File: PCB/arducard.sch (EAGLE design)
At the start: 93 parts, among them J1 USB MICRO, J3 051296-4094, J4 M02PTH, Q1 BSS84, Q10 DMG2301U-7, Q2 BC817-16LT1SMD, Q3 DMG2301U-7, Q4 2N7002, Q5 BSS84, Q6 2N7002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

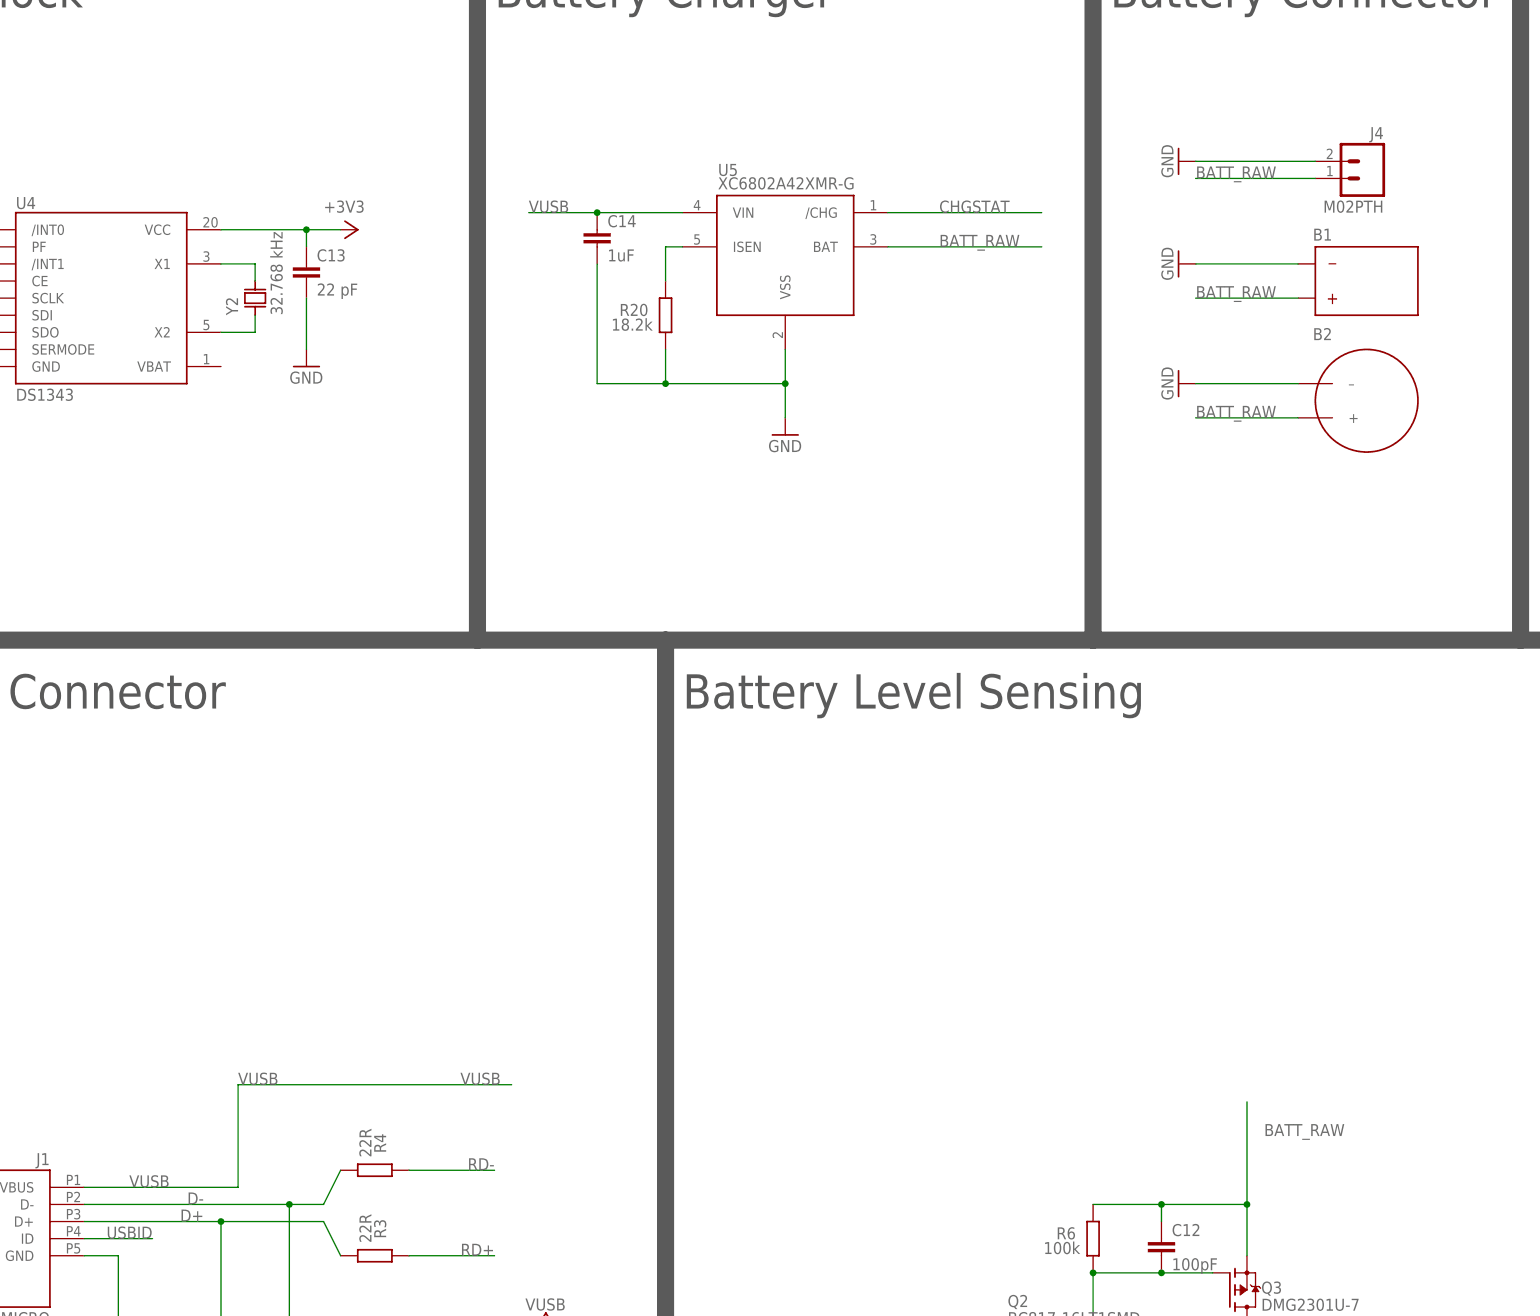
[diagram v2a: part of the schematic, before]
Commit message: removed flat cell battery connector
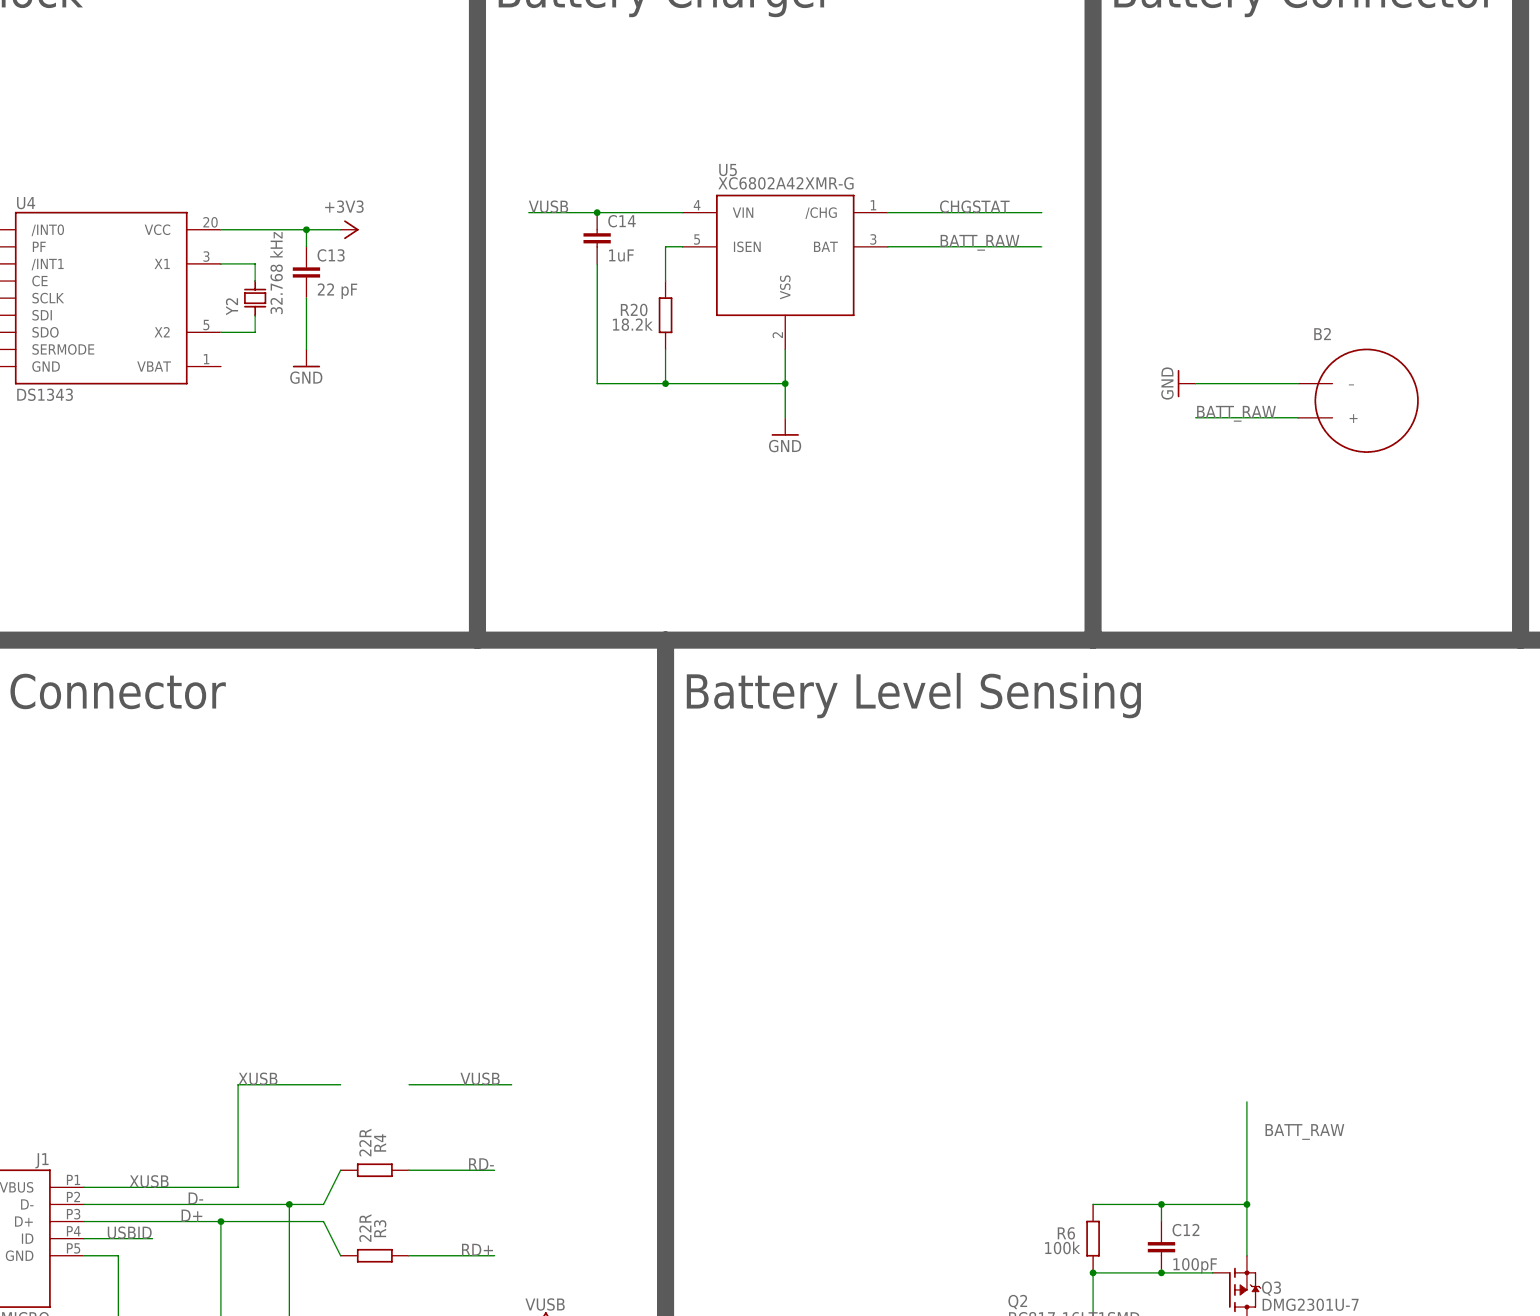
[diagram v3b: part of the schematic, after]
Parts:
- removed B1: PGEB016144, arducard-battery:PGEB016144
- removed J4: M02PTH, SparkFun-Connectors:M02PTH
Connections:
- new net XUSB: J1.VBUS
- net BATT_RAW: no longer B1.+, J4.1
- net GND: no longer B1.-, J4.2
- net VUSB: no longer J1.VBUS
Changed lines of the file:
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@@
 <part name="GND28" library="supply1" deviceset="GND" device=""/>
 <part name="R20" library="SmartPrj" deviceset="R-EU_" device="R0603" value="18.2k"/>
-<part name="GND9" library="supply1" deviceset="GND" device=""/>
-<part name="J4" library="SparkFun-Connectors" deviceset="M02" device="PTH"/>
-<part name="GND10" library="supply1" deviceset="GND" device=""/>
 <part name="GND4" library="supply1" deviceset="GND" device=""/>
 <part name="GND29" library="supply1" deviceset="GND" device=""/>
@@
 <part name="U5" library="arducard-xc6802" deviceset="XC6802A42XMR-G" device=""/>
 <part name="U2" library="v-reg-micrel" deviceset="MIC5219XX" device=""/>
-<part name="B1" library="arducard-battery" deviceset="PGEB016144" device=""/>
 <part name="B2" library="arducard-coincell" deviceset="LIR2016" device=""/>
 <part name="U$1" library="MyPOW" deviceset="VUSB" device=""/>
@@
 <attribute name="VALUE" x="343.535" y="240.792" size="1.778" layer="96" rot="R180"/>
 </instance>
-<instance part="GND9" gate="1" x="421.64" y="248.92" rot="R270"/>
-<instance part="J4" gate="G$1" x="449.58" y="261.62" rot="MR0"/>
-<instance part="GND10" gate="1" x="421.64" y="264.16" rot="R270"/>
 <instance part="GND4" gate="1" x="83.82" y="81.28" rot="R270"/>
 <instance part="GND29" gate="1" x="81.28" y="116.84"/>
@@
 <instance part="U5" gate="XC6802A42XMR-G" x="363.22" y="254"/>
 <instance part="U2" gate="G1" x="543.56" y="243.84"/>
-<instance part="B1" gate="G$1" x="449.58" y="246.38"/>
 <instance part="B2" gate="G$1" x="449.58" y="228.6"/>
 <instance part="U$1" gate="G$1" x="495.3" y="251.46"/>
@@
 <junction x="345.44" y="231.14"/>
 <pinref part="U5" gate="XC6802A42XMR-G" pin="VSS"/>
-</segment>
-<segment>
-<pinref part="GND9" gate="1" pin="GND"/>
-<wire x1="424.18" y1="248.92" x2="439.42" y2="248.92" width="0.1524" layer="91"/>
-<pinref part="B1" gate="G$1" pin="-"/>
-</segment>
-<segment>
-<pinref part="J4" gate="G$1" pin="2"/>
-<pinref part="GND10" gate="1" pin="GND"/>
-<wire x1="441.96" y1="264.16" x2="424.18" y2="264.16" width="0.1524" layer="91"/>
 </segment>
 <segment>
@@
 </segment>
 </net>
-<net name="VUSB" class="3">
+<net name="VUSB" class="0">
 <segment>
 <wire x1="114.3" y1="60.96" x2="104.14" y2="60.96" width="0.1524" layer="91"/>
@@
 </segment>
 <segment>
+<wire x1="322.58" y1="127" x2="307.34" y2="127" width="0.1524" layer="91"/>
+<label x="314.96" y="127" size="1.778" layer="95"/>
+</segment>
+<segment>
 <wire x1="347.98" y1="256.54" x2="335.28" y2="256.54" width="0.1524" layer="91"/>
 <pinref part="C14" gate="G$1" pin="1"/>
@@
 <pinref part="U$12" gate="G$1" pin="VUSB"/>
 <wire x1="518.16" y1="259.08" x2="518.16" y2="261.62" width="0.1524" layer="91"/>
-</segment>
-<segment>
-<wire x1="281.94" y1="111.76" x2="281.94" y2="127" width="0.1524" layer="91"/>
-<wire x1="281.94" y1="127" x2="322.58" y2="127" width="0.1524" layer="91"/>
-<wire x1="259.08" y1="111.76" x2="281.94" y2="111.76" width="0.1524" layer="91"/>
-<label x="271.78" y="111.76" size="1.778" layer="95" rot="MR0"/>
-<label x="281.94" y="127" size="1.778" layer="95"/>
-<pinref part="J1" gate="G$1" pin="VBUS"/>
-<label x="314.96" y="127" size="1.778" layer="95"/>
 </segment>
 </net>
@@
 <pinref part="J1" gate="G$1" pin="D+"/>
 <pinref part="R3" gate="G$1" pin="1"/>
+</segment>
+</net>
+<net name="XUSB" class="3">
+<segment>
+<wire x1="281.94" y1="111.76" x2="281.94" y2="127" width="0.1524" layer="91"/>
+<wire x1="281.94" y1="127" x2="297.18" y2="127" width="0.1524" layer="91"/>
+<wire x1="259.08" y1="111.76" x2="281.94" y2="111.76" width="0.1524" layer="91"/>
+<label x="271.78" y="111.76" size="1.778" layer="95" rot="MR0"/>
+<label x="281.94" y="127" size="1.778" layer="95"/>
+<pinref part="J1" gate="G$1" pin="VBUS"/>
 </segment>
 </net>
@@
 </segment>
 <segment>
-<wire x1="439.42" y1="243.84" x2="424.18" y2="243.84" width="0.1524" layer="91"/>
-<label x="424.18" y="243.84" size="1.778" layer="95"/>
-<pinref part="B1" gate="G$1" pin="+"/>
-</segment>
-<segment>
-<pinref part="J4" gate="G$1" pin="1"/>
-<wire x1="441.96" y1="261.62" x2="424.18" y2="261.62" width="0.1524" layer="91"/>
-<label x="424.18" y="261.62" size="1.778" layer="95"/>
-</segment>
-<segment>

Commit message: initial routing for dorkbot
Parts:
- removed L1: MH2029-300Y, wuerth-elektronik:WE-CBF_0805
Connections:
- removed net N$10: C10.1, D1.C, Q1.S, U2.EN, U2.IN
- removed net XUSB: J1.VBUS
- new net 5V: C10.1, C14.1, D1.C, Q1.S, U1.VBUS, U2.EN, U2.IN, U5.VIN
- net GND: no longer L1.1, L1.2
- net VUSB: now also J1.VBUS; no longer C14.1, U1.VBUS, U5.VIN
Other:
- note removed: "MicroSD Connector"
- moved on the sheet: D1, SW0, SW1, SW2, SW3, SW4

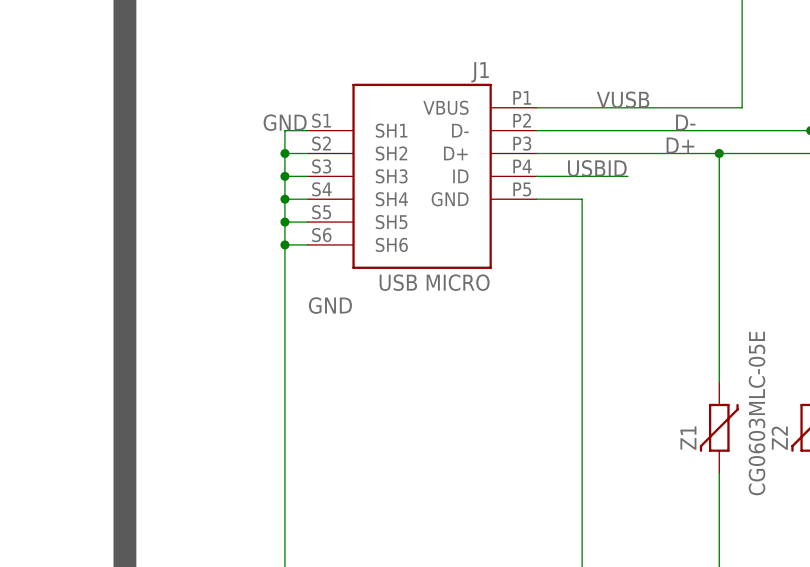
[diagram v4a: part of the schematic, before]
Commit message: renamed a part
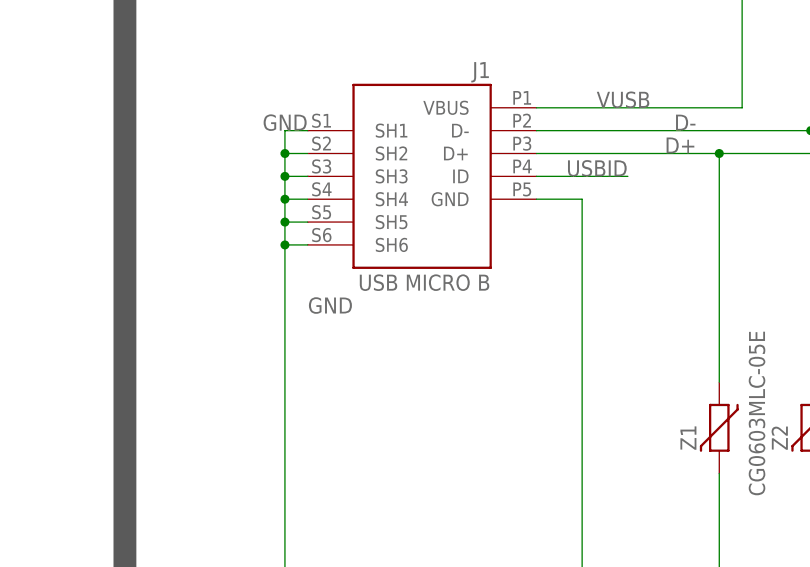
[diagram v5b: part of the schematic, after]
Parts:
- J1: value USB MICRO -> USB MICRO B
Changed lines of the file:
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@@
 <part name="C9" library="SmartPrj" deviceset="C-EU" device="C0603" value="100n"/>
 <part name="GND8" library="supply1" deviceset="GND" device=""/>
-<part name="J1" library="SmartPrj" deviceset="MYCON2_USB-MINI-B" device="" value="USB MICRO"/>
+<part name="J1" library="SmartPrj" deviceset="MYCON2_USB-MINI-B" device="" value="USB MICRO B"/>
 <part name="+3V1" library="supply1" deviceset="+3V3" device=""/>
 <part name="+3V2" library="supply1" deviceset="+3V3" device=""/>
